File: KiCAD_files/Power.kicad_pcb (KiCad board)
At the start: 2 copper layers, 90 x 100 mm, 84 parts, among them J1 2604-1102, J2 2604-1102, J3 Power_Board_outline, J4 2604-1102, J5 2604-1102, Q1 QM6006D, Q2 QM6006D, Q3 Q_NIGBT_GCE, Q4 QM6006D, Q5 QM6006D, U1 ACS730xLCTR-20AB, U2 LM35-LP, U3 ACS712xLCTR-20A, U4 ACS730xLCTR-20AB

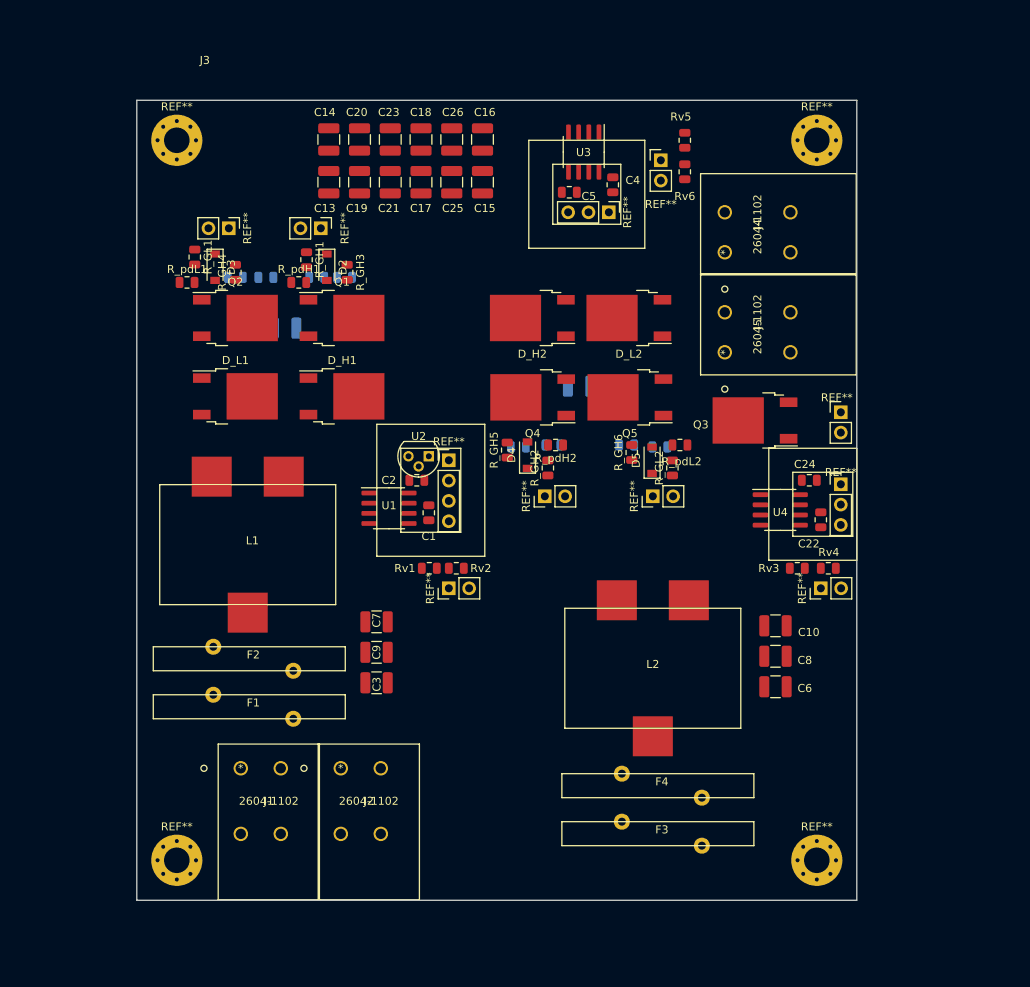
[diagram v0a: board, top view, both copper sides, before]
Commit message: Added alpha version of Nucleo Shield stage - Routed power board
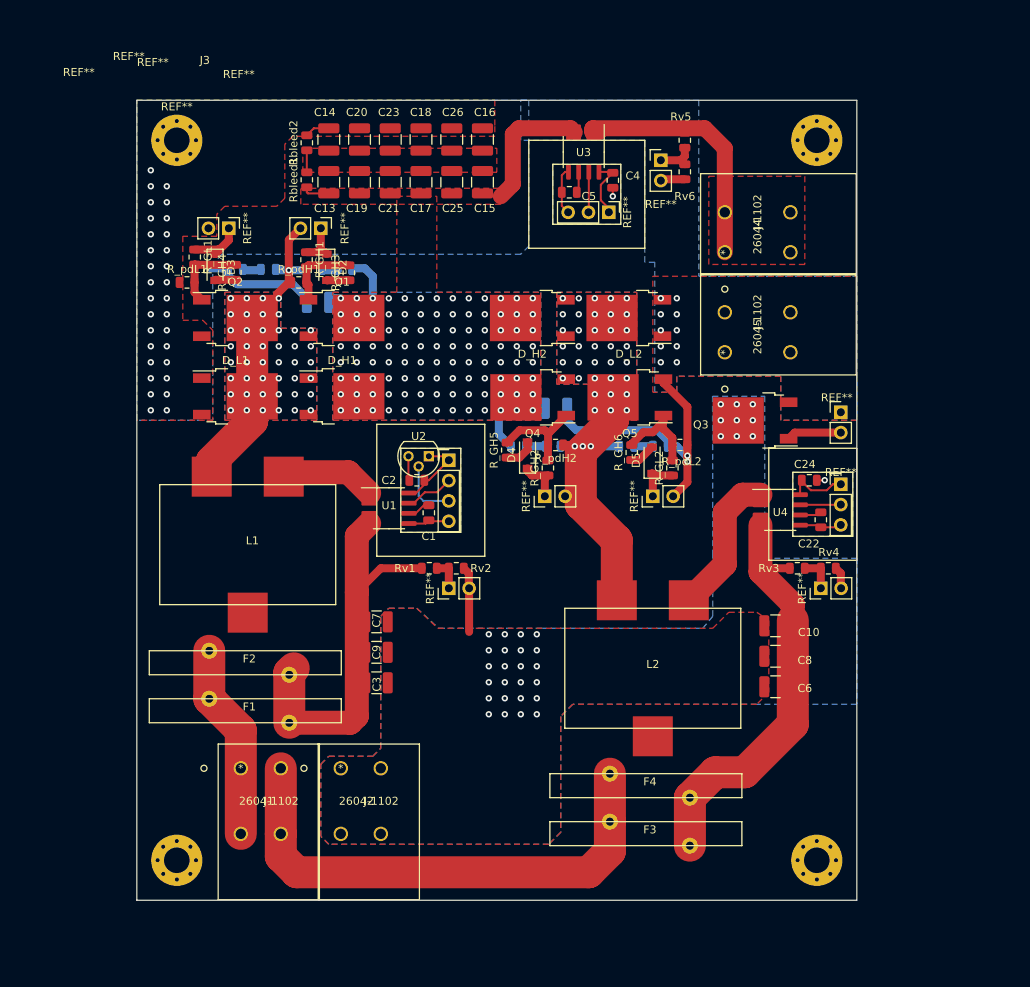
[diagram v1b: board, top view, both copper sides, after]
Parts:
- added Rbleed1: 1M, Resistor_SMD:R_0805_2012Metric, F.Cu at (63.2, 51.9)
- added Rbleed2: 1M, Resistor_SMD:R_0805_2012Metric, F.Cu at (63.2, 47.3)
- moved C11 5.23 mm to (64.7, 67.2)
- moved C12 3.99 mm to (94.4, 80.5)
- moved F3 1.50 mm to (106.1, 133.7)
- moved F4 1.50 mm to (106.1, 127.7)
- moved R_2snub1 1.04 mm to (58.4, 63.1), turned to 180 degrees
- moved C_1snub1 1.04 mm to (64.2, 63.1), turned to 180 degrees
- moved C_2snub1 1.00 mm to (54.3, 63.1)
- moved R_1snub1 1.00 mm to (68.0, 63.1)
- moved F1 0.71 mm to (56.1, 118.3)
- moved F2 0.71 mm to (56.1, 112.3)
- moved C4 0.56 mm to (101.5, 52.0)
- moved R_GH3 0.21 mm to (68.5, 63.6), turned to 90 degrees
- moved C_1snub2 0.16 mm to (94.0, 85.2)
- moved R_2snub2 0.16 mm to (103.2, 85.2)
- moved C_2snub2 0.10 mm to (107.4, 85.2)
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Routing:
- net Net-(F3-Pad2): track 0.00 -> 63.7 mm
- net GNDREF: track 0.00 -> 56.8 mm, vias 0 -> 43
- net /V_In2: track 0.00 -> 53.1 mm
- net /V_In1: track 0.00 -> 49.9 mm
- net /SW_Node2: track 0.00 -> 38.8 mm, vias 0 -> 39
- net /SW_Node1: track 0.00 -> 35.9 mm, vias 0 -> 45
- net /V_Out: track 0.00 -> 34.4 mm, vias 0 -> 104
- net Net-(J4-Pad1): track 0.00 -> 31.9 mm
- net +5VD: track 0.00 -> 24.6 mm
- net Net-(F1-Pad2): track 0.00 -> 24.5 mm
- net /DGND: track 0.00 -> 21.6 mm, vias 0 -> 2
- net Net-(L2-Pad1): track 0.00 -> 18.2 mm
- net Net-(Q4-Pad1): track 0.00 -> 12.5 mm
- net Net-(Q5-Pad1): track 0.00 -> 12.2 mm
- net Net-(L1-Pad1): track 0.00 -> 12.0 mm
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- added copper zone on B.Cu, net /DGND
- added copper zone on B.Cu, net /N
- added copper zone on F.Cu, net /N
- added copper zone on B.Cu, net /SW_Node1
- added copper zone on F.Cu, net /SW_Node1
- added copper zone on B.Cu, net /SW_Node2
- added copper zone on F.Cu, net /SW_Node2
- added copper zone on B.Cu, net /V_Out
- added copper zone on F.Cu, net /V_Out
- added copper zone on B.Cu, net GNDREF
- added copper zone on F.Cu, net GNDREF
- added copper zone on F.Cu, net Net-(C13-Pad2)
- added copper zone on F.Cu, net Net-(J4-Pad1)

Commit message: Improved power board traces - Took a power electronic routing guideline into consideration.
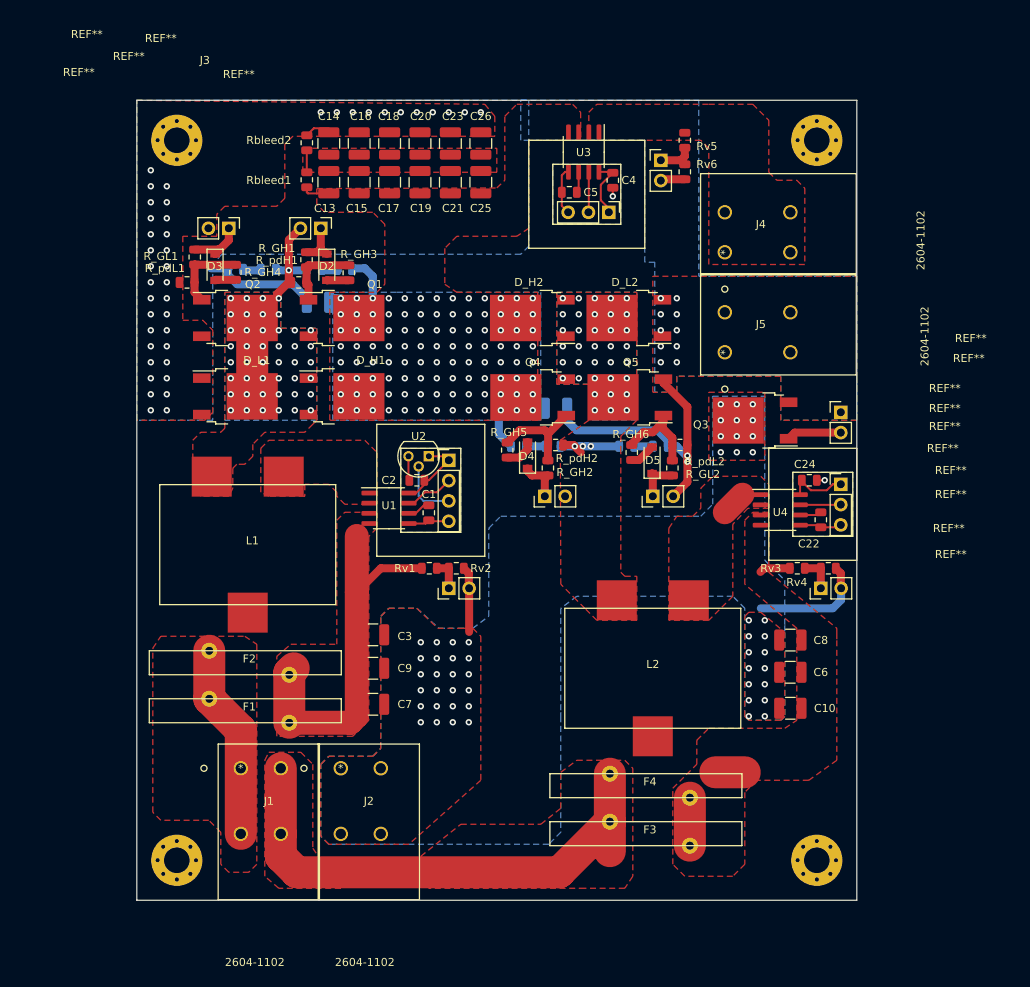
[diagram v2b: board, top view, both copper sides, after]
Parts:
- C10, C13, C14, C15, C16, C17, C18, C19, C20, C21, C23, C25, C26, C3, C6, C7, C8, C9: value 100nF -> 4.7uF
- moved C16 15.4 mm to (69.8, 47.4)
- moved C15 15.4 mm to (69.8, 52.2)
- moved C10 10.5 mm to (123.7, 118.0)
- moved C7 10.3 mm to (71.5, 117.5)
- moved C20 7.57 mm to (77.4, 47.4)
- moved C19 7.56 mm to (77.4, 52.2)
- moved C23 7.53 mm to (81.2, 47.4)
- moved C21 7.52 mm to (81.2, 52.2)
- moved C3 6.02 mm to (71.5, 108.8)
- moved C18 3.96 mm to (73.6, 47.4)
- moved C17 3.93 mm to (73.6, 52.2)
- moved C26 3.67 mm to (85.0, 47.4)
- moved C25 3.63 mm to (85.0, 52.2)
- moved C8 2.75 mm to (123.7, 109.5)
- moved C6 2.60 mm to (123.7, 113.5)
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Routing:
- net /V_In2: track 53.1 -> 13.5 mm
- net Net-(J4-Pad1): track 31.9 -> 0.00 mm
- net /SW_Node2: track 38.8 -> 9.93 mm
- net /V_Out: track 34.4 -> 17.8 mm
- net Net-(L2-Pad1): track 18.2 -> 3.11 mm
- net /SW_Node1: track 35.9 -> 23.8 mm
- net /N: track 11.0 -> 22.9 mm, vias 33 -> 50
- net Net-(L1-Pad1): track 12.0 -> 0.77 mm
- net /V_In1: track 49.9 -> 47.7 mm
- net Net-(F3-Pad2): track 63.7 -> 65.3 mm
- net GNDREF: vias 43 -> 54
- added copper zone on F.Cu, net /V_In1
- added copper zone on F.Cu, net /V_In2
- added copper zone on F.Cu, net Net-(F1-Pad2)
- added copper zone on F.Cu, net Net-(F3-Pad2)
- added copper zone on F.Cu, net Net-(L1-Pad1)
- added copper zone on F.Cu, net Net-(L2-Pad1)

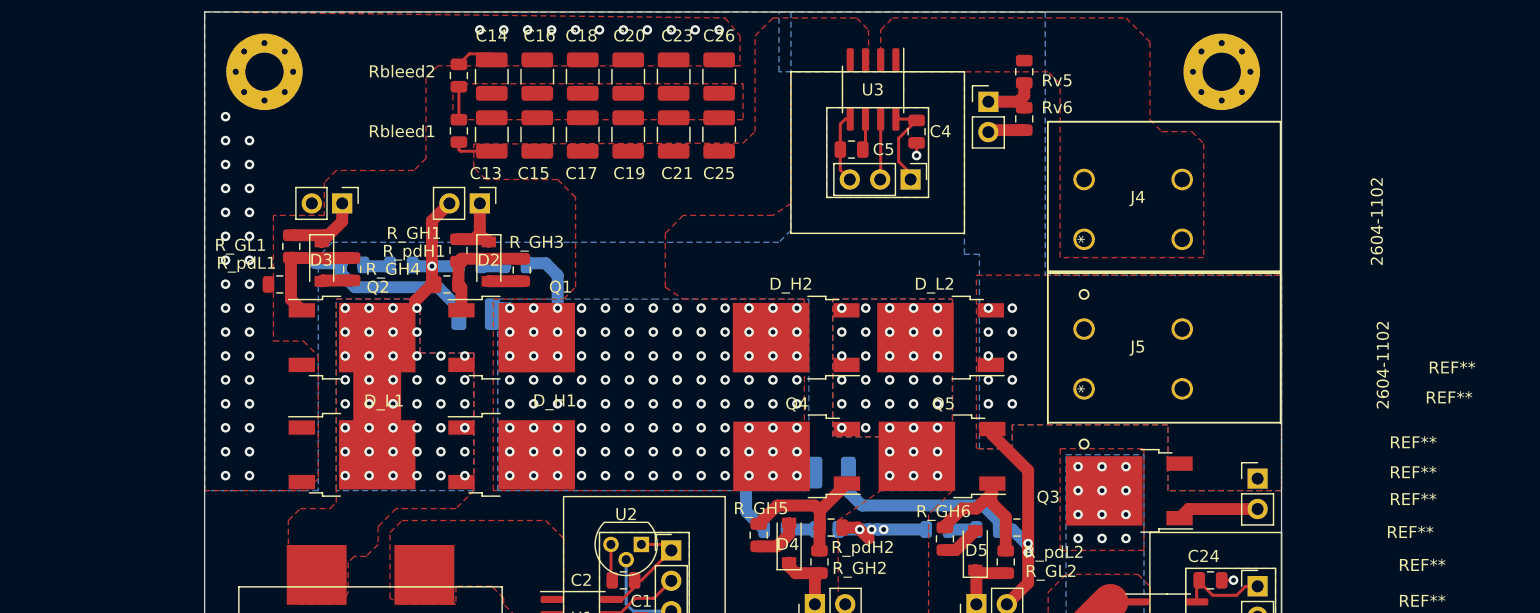
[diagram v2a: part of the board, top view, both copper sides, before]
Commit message: Added heatsink holes and bottom mask for the power baord.
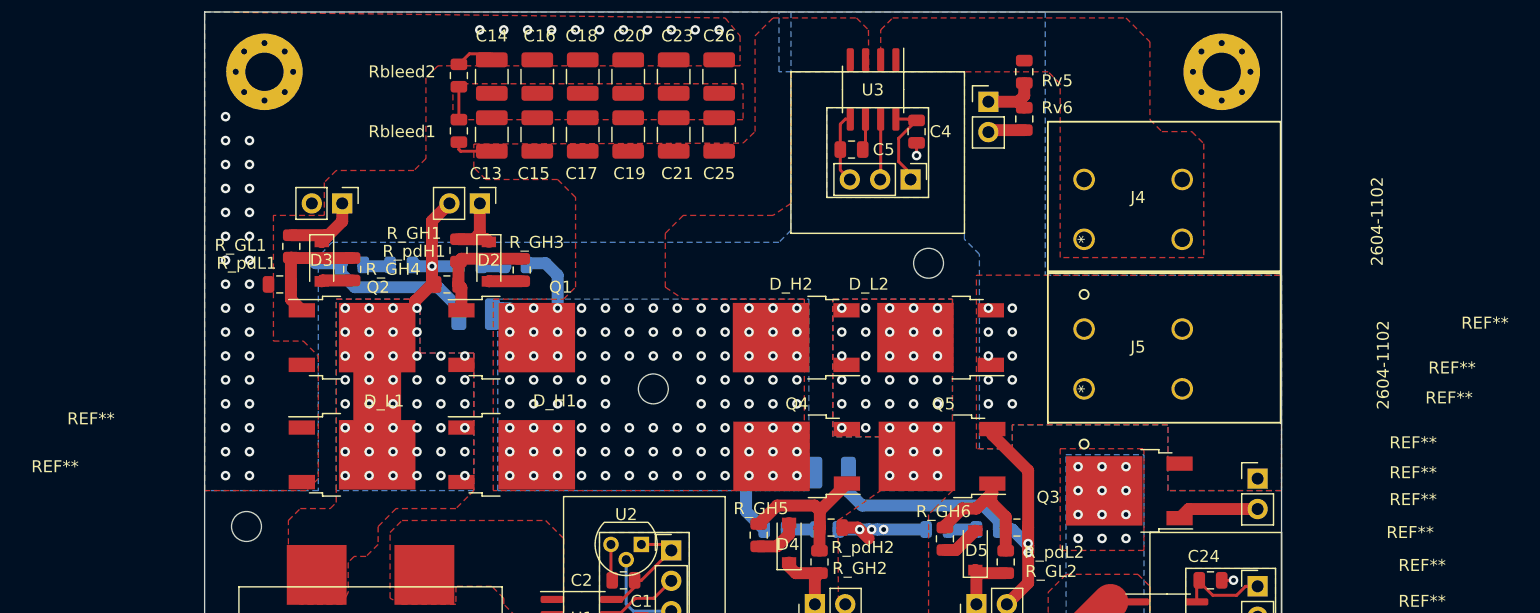
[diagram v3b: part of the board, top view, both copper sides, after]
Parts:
- added REF**: MountingHole_2.5mm, MountingHole:MountingHole_2.5mm, F.Cu at (102.5, 63.0)
- added REF**: MountingHole_2.5mm, MountingHole:MountingHole_2.5mm, F.Cu at (79.5, 73.5)
- added REF**: MountingHole_2.5mm, MountingHole:MountingHole_2.5mm, F.Cu at (45.5, 85.0)
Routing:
- net GNDREF: vias 54 -> 52
- net /V_Out: vias 104 -> 98
- net (no net): vias 0 -> 2

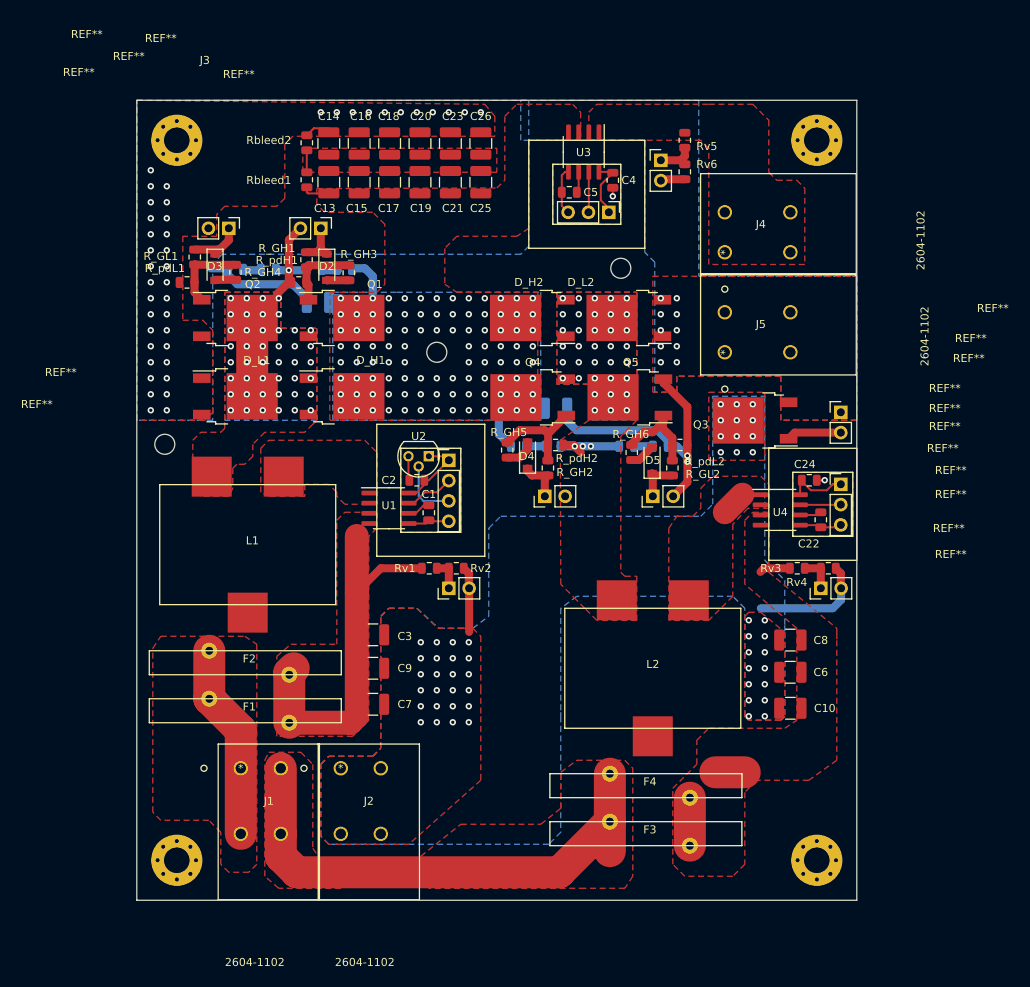
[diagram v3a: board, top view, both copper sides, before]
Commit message: Added optional film caps - Added Heatsink mounting holes Verified mezzanine electrical connexions.
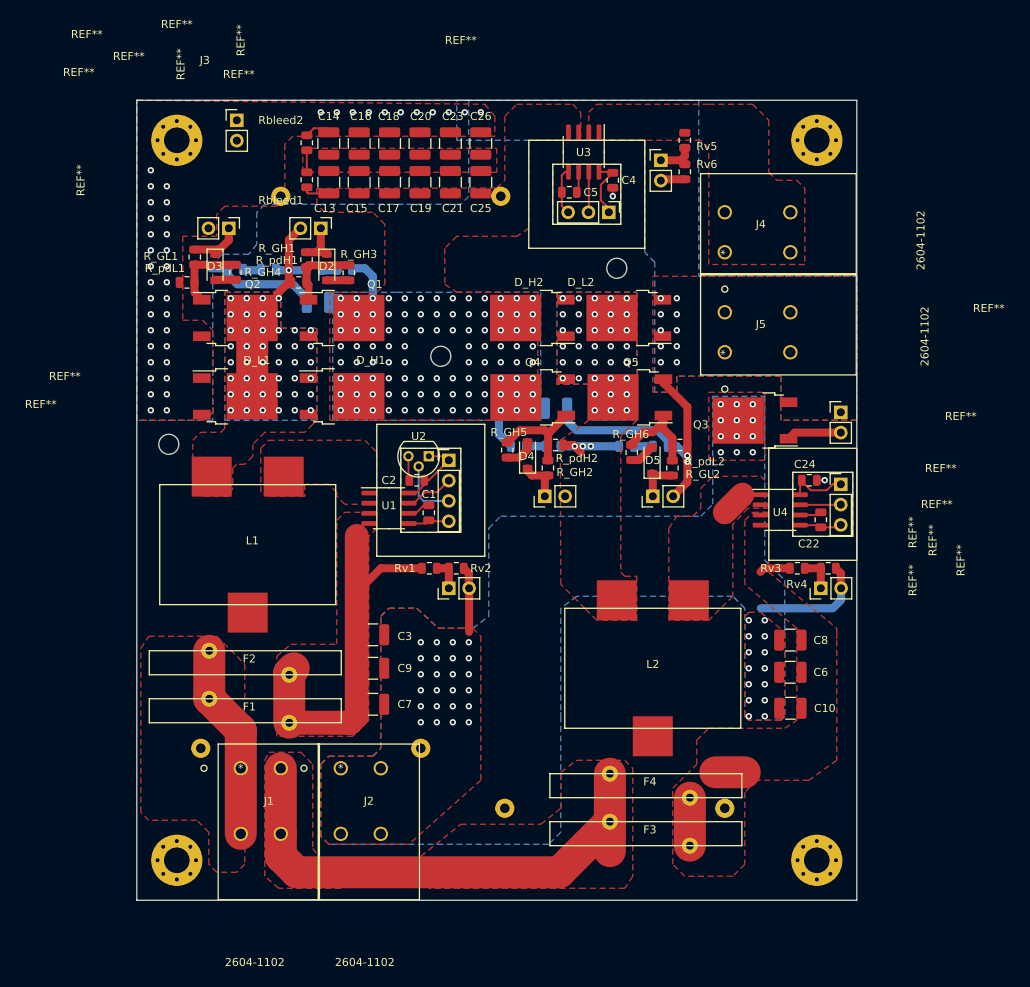
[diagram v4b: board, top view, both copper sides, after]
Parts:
- removed the REF** at (102.5, 63.0)
- removed the REF** at (79.5, 73.5)
- added CFilm1: C_Rect_L31.5mm_W20.0mm_P27.50mm_MKS4, Capacitor_THT:C_Rect_L31.5mm_W20.0mm_P27.50mm_MKS4, B.Cu at (77.5, 123.0)
- added CFilm2: C_Rect_L31.5mm_W20.0mm_P27.50mm_MKS4, Capacitor_THT:C_Rect_L31.5mm_W20.0mm_P27.50mm_MKS4, B.Cu at (88.0, 130.5)
- added CFilmOut: C_Rect_L31.5mm_W20.0mm_P27.50mm_MKS4, Capacitor_THT:C_Rect_L31.5mm_W20.0mm_P27.50mm_MKS4, B.Cu at (60.0, 54.0)
- added REF**: MountingHole_2.5mm, MountingHole:MountingHole_2.5mm, F.Cu at (102.0, 63.0)
- added REF**: MountingHole_2.5mm, MountingHole:MountingHole_2.5mm, F.Cu at (80.0, 74.0)
- moved REF** 0.50 mm to (46.0, 85.0)
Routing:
- net GNDREF: vias 52 -> 54
- net (no net): vias 2 -> 0

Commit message: Finalized BOM - Added mezzanine connectors overlay - Improved Nucleo shield
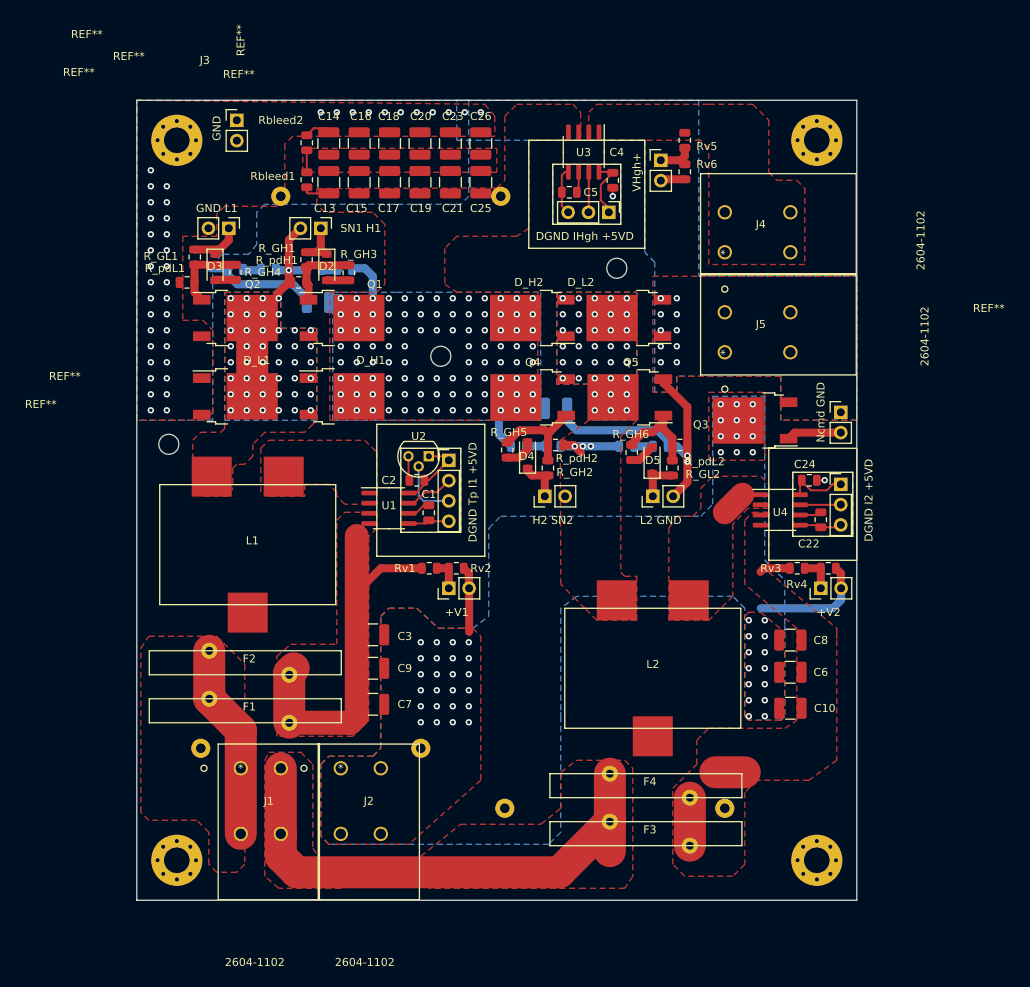
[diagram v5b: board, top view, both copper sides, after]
